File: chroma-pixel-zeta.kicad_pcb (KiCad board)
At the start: 4 copper layers, 138 x 93.2 mm, 151 parts, among them J1 Micro_SD_Card_Det_Hirose_DM3AT, J10 Conn_01x24_MountingPin, J11 AudioJack3, J12 USB_A, J14 LCD_TP_I2C, J15 LCD_SPI, J2 TFT_LCD, J4 USB-C, J5 I2C-STEMMA-QT, J6 BAT, J7 swd, J8 SPKR, J9 UART, SW1 SW_Push, SW2 SW_Push, SW3 SW_Push, SW4 SW_Push, U1 MT25Q, U10 PCM5102A, U11 TLV75733PDBV, U2 STM32H743IITx, U4 MT25Q, U5 TPS61169, U6 MAX98357AETE_, U7 CAT24C128, U8 TLV75733PDBV, U9 MT48LC16M16A2P, Y1 25MHz, Y2 32.768KHz

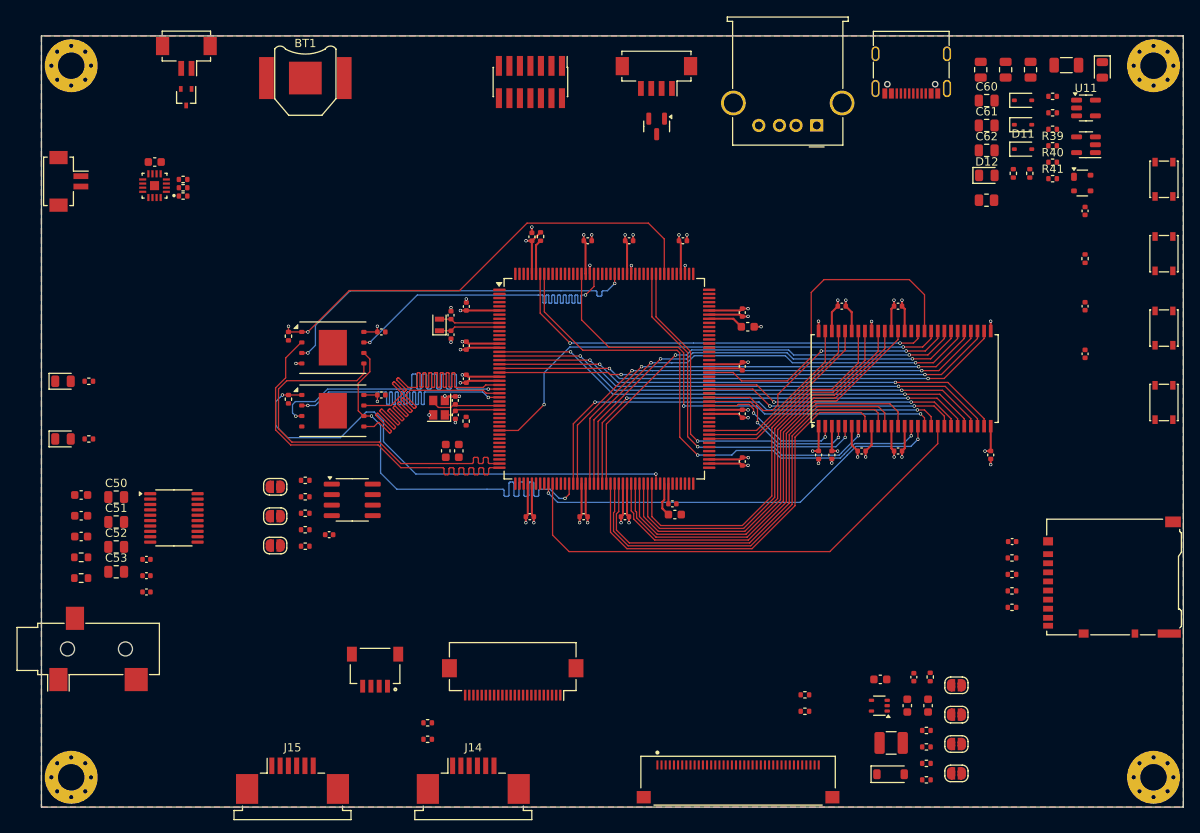
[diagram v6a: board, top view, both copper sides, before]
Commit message: finished layout backlight driver
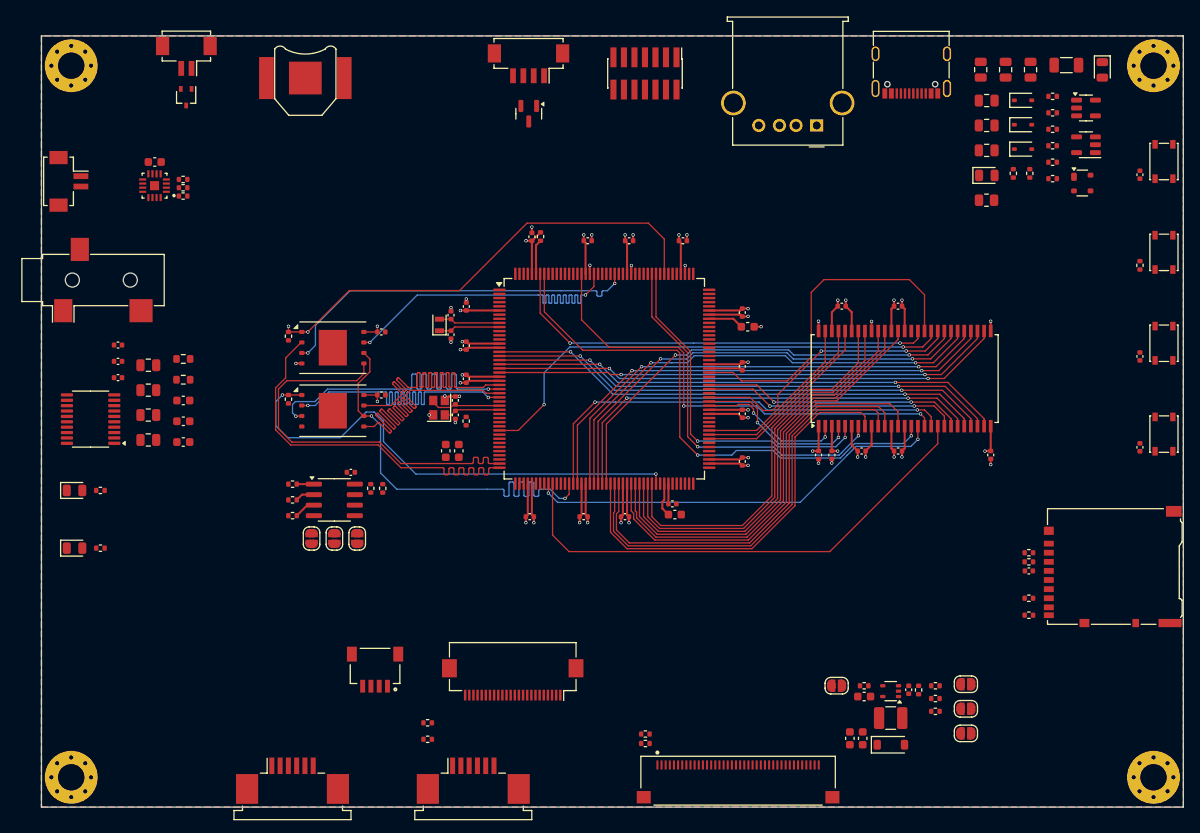
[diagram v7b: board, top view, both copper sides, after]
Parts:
- moved J11 44.6 mm to (84.8, 71.8)
- moved C59 30.0 mm to (87.9, 79.7), turned to 180 degrees
- moved R38 29.2 mm to (95.7, 81.4), turned to 180 degrees
- moved C57 26.1 mm to (87.9, 81.7), turned to 180 degrees
- moved C53 25.3 mm to (91.5, 82.1), turned to 180 degrees
- moved R37 24.8 mm to (95.7, 83.9), turned to 180 degrees
- moved C55 22.2 mm to (87.9, 83.6), turned to 180 degrees
- moved C58 20.6 mm to (95.7, 86.4), turned to 180 degrees
- moved R35 19.9 mm to (151.6, 126.7)
- moved R36 19.7 mm to (151.6, 127.8)
- moved C52 19.3 mm to (91.5, 85.1), turned to 180 degrees
- moved C56 16.8 mm to (95.7, 88.9), turned to 180 degrees
- moved U10 15.6 mm to (84.5, 88.6), turned to 180 degrees
- moved D9 15.5 mm to (137.5, 51.7)
- moved J9 15.5 mm to (137.5, 45.7)
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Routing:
- net Net-(JP7-A): track 0.00 -> 2.59 mm
- net Net-(JP6-A): track 0.00 -> 2.33 mm
- net Net-(JP5-A): track 0.00 -> 2.06 mm

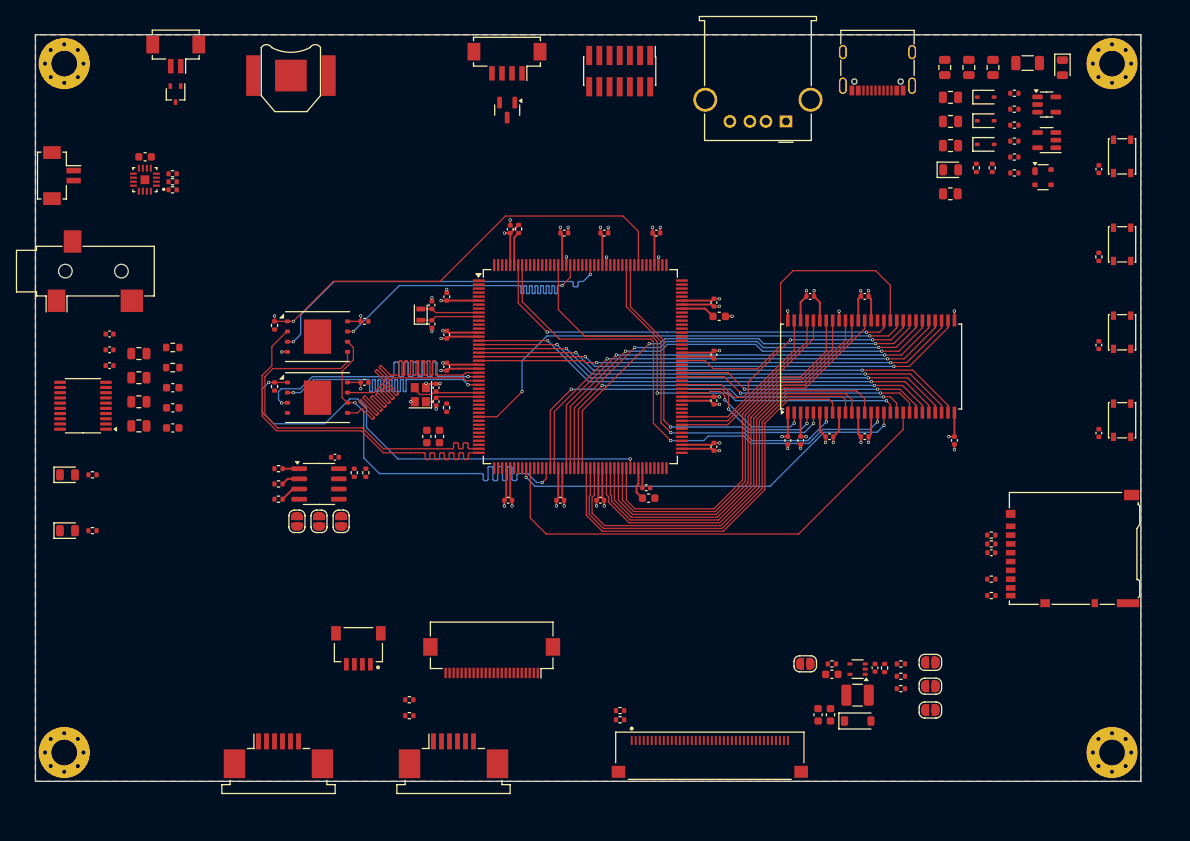
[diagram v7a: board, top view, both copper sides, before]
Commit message: Changes: USB C to midmount, CR1220 socket, flip MCU to shorten the LCD traces
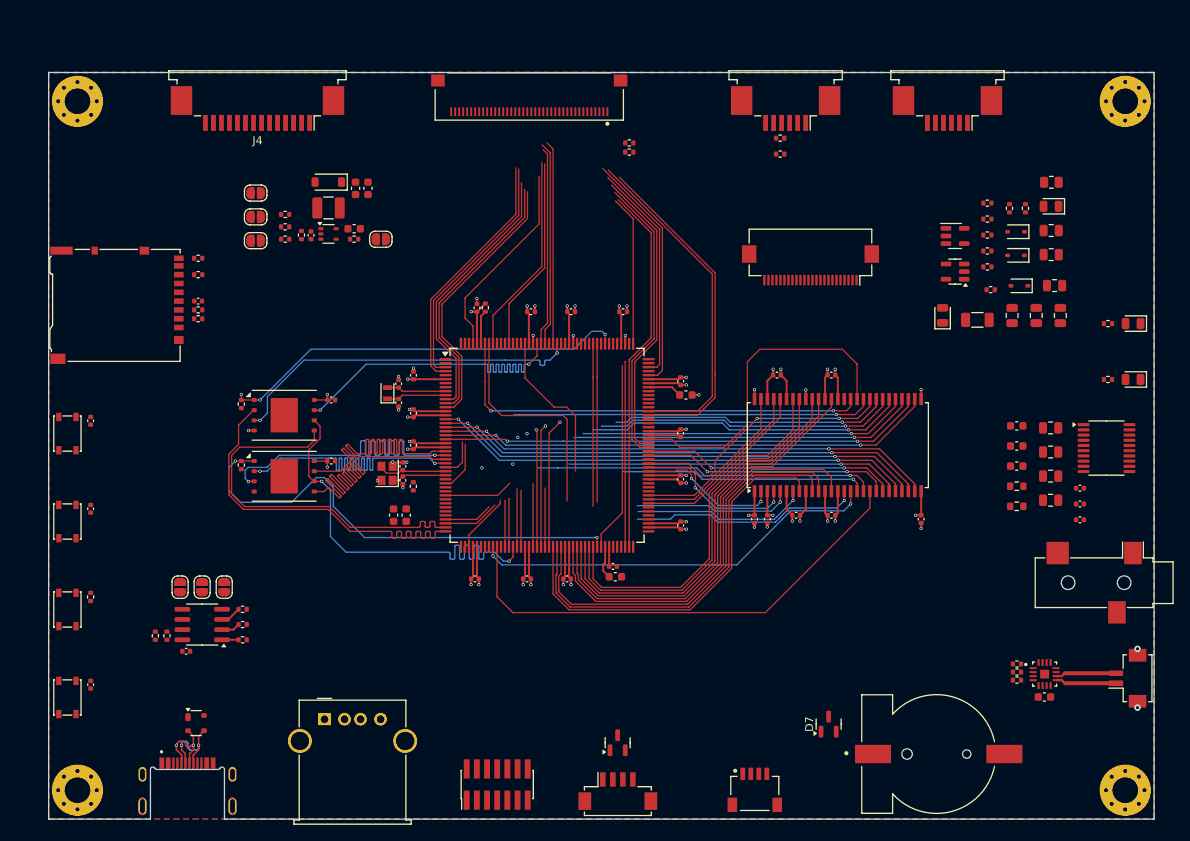
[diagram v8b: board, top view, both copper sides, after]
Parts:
- removed BT1: Battery_Cell, Battery:BatteryHolder_Keystone_2998_1x6.8mm
- removed J6: BAT, Connector_Hirose:Hirose_DF13C_CL535-0402-2-51_1x02-1MP_P1.25mm_Vertical
- added BT2: S8411-45R, CR1220-Batt-conn-S8411-45R:CR1220-Batt-conn-S8411-45R, F.Cu at (191.1, 132.1)
- added J3: 2169900003, USB_C_Mid_mount_MOLEX_2169900003:USB_C_Mid_mount_MOLEX_2169900003, F.Cu at (97.6, 138.6)
- D7: footprint Package_TO_SOT_SMD:SOT-323_SC-70 -> Package_TO_SOT_SMD:SOT-23
- J4: value USB-C -> SPI_LCD; footprint Connector_USB:USB_C_Receptacle_G-Switch_GT-USB-7010ASV -> Connector_FFC-FPC:TE_1-84953-4_1x14-1MP_P1.0mm_Horizontal
- moved H1 160.5 mm to (214.6, 136.6), turned to 0 degrees
- moved H4 157.8 mm to (83.8, 136.6), turned to -90 degrees
- moved H2 155.4 mm to (214.6, 50.6), turned to 0 degrees
- moved H3 152.6 mm to (83.8, 50.6), turned to 180 degrees
- moved SW1 148.0 mm to (82.6, 125.1), turned to -90 degrees
- moved J8 147.1 mm to (214.9, 122.7), turned to 90 degrees
- moved C24 141.4 mm to (85.5, 123.5), turned to -90 degrees
- moved SW2 139.3 mm to (82.6, 114.1), turned to -90 degrees
- moved D6 135.5 mm to (215.6, 78.4), turned to 180 degrees
- moved SW3 133.8 mm to (82.6, 103.1), turned to -90 degrees
- moved D5 133.6 mm to (215.6, 85.4), turned to 180 degrees
- moved J11 133.0 mm to (212.0, 110.7), turned to -90 degrees
- moved R18 132.8 mm to (85.5, 112.5), turned to -90 degrees
- moved SW4 131.7 mm to (82.6, 92.1), turned to -90 degrees
- moved C23 131.0 mm to (204.6, 125.0), turned to 180 degrees
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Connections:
- J14 pad 1: unconnected-(J14-Pin_1-Pad1) -> GND
- J14 pad 2: unconnected-(J14-Pin_2-Pad2) -> /LCD/LCD_TP_INT
- J14 pad 3: unconnected-(J14-Pin_3-Pad3) -> /LCD/LCD_TP_RST
- J14 pad 4: unconnected-(J14-Pin_4-Pad4) -> +3V3
- J14 pad 5: unconnected-(J14-Pin_5-Pad5) -> /LCD/LCD_TP_SCL
- J14 pad 6: unconnected-(J14-Pin_6-Pad6) -> /LCD/LCD_TP_SDA
- J14 pad MP: unconnected-(J14-MountPin-PadMP) -> GND
- J2 pad 13: /LCD/LCD_B7 -> /LCD/LTDC_B7
- J2 pad 14: /LCD/LCD_B6 -> /LCD/LTDC_B6
- J2 pad 15: /LCD/LCD_B5 -> /LCD/LTDC_B5
- J2 pad 16: /LCD/LCD_B4 -> /LCD/LTDC_B4
- J2 pad 17: /LCD/LCD_B3 -> /LCD/LTDC_B3
- J2 pad 18: /LCD/LCD_B2 -> /LCD/LTDC_B2
- J2 pad 19: /LCD/LCD_B1 -> /LCD/LTDC_B1
- J2 pad 20: /LCD/LCD_B0 -> /LCD/LTDC_B0
- J2 pad 21: /LCD/LCD_G7 -> /LCD/LTDC_G7
- J2 pad 22: /LCD/LCD_G6 -> /LCD/LTDC_G6
- J2 pad 23: /LCD/LCD_G5 -> /LCD/LTDC_G5
- J2 pad 24: /LCD/LCD_G4 -> /LCD/LTDC_G4
- J2 pad 25: /LCD/LCD_G3 -> /LCD/LTDC_G3
- J2 pad 26: /LCD/LCD_G2 -> /LCD/LTDC_G2
- J2 pad 27: /LCD/LCD_G1 -> /LCD/LTDC_G1
- J2 pad 28: /LCD/LCD_G0 -> /LCD/LTDC_G0
- J2 pad 29: /LCD/LCD_R7 -> /LCD/LTDC_R7
- J2 pad 30: /LCD/LCD_R6 -> /LCD/LTDC_R6
- J2 pad 31: /LCD/LCD_R5 -> /LCD/LTDC_R5
- J2 pad 32: /LCD/LCD_R4 -> /LCD/LTDC_R4
- J2 pad 33: /LCD/LCD_R3 -> /LCD/LTDC_R3
- J2 pad 34: /LCD/LCD_R2 -> /LCD/LTDC_R2
- J2 pad 35: /LCD/LCD_R1 -> /LCD/LTDC_R1
- J2 pad 36: /LCD/LCD_R0 -> /LCD/LTDC_R0
- R11 pad 1: GND -> Net-(J3-CC2)
- R11 pad 2: Net-(J4-CC1) -> GND
- R12 pad 2: Net-(J4-CC2) -> Net-(J3-CC1)
- R33 pad 2: /LCD/LCD_TP_SCL -> /LCD/LCD_TP_SDA
- R34 pad 2: /LCD/LCD_TP_SDA -> /LCD/LCD_TP_SCL
- U2 pad 100: unconnected-(U2-PD12-Pad100) -> /AUDIO/DIN
- U2 pad 11: unconnected-(U2-PI9-Pad11) -> /LCD/LTDC_VSYNC
- U2 pad 110: unconnected-(U2-PG6-Pad110) -> /LCD/LTDC_R7
- U2 pad 111: unconnected-(U2-PG7-Pad111) -> /LCD/LTDC_CLK
- U2 pad 118: unconnected-(U2-PC9-Pad118) -> /LCD/LTDC_G3
- U2 pad 119: unconnected-(U2-PA8-Pad119) -> /LCD/LTDC_B3
- U2 pad 12: unconnected-(U2-PI10-Pad12) -> /LCD/LTDC_HSYNC
- U2 pad 122: unconnected-(U2-PA11-Pad122) -> /USB/USB_D-
- U2 pad 123: unconnected-(U2-PA12-Pad123) -> /USB/USB_D+
- U2 pad 128: unconnected-(U2-PH13-Pad128) -> /LCD/LTDC_G2
- U2 pad 13: unconnected-(U2-PI11-Pad13) -> /LCD/LTDC_G6
- U2 pad 130: unconnected-(U2-PH15-Pad130) -> /LCD/LTDC_G4
- U2 pad 133: unconnected-(U2-PI2-Pad133) -> /LCD/LTDC_G7
- U2 pad 138: unconnected-(U2-PA15-Pad138) -> /AUDIO/LRCK
- U2 pad 139: unconnected-(U2-PC10-Pad139) -> /AUDIO/BCK
- U2 pad 151: unconnected-(U2-PD7-Pad151) -> /AUDIO/I2S_SDO
- U2 pad 153: unconnected-(U2-PG10-Pad153) -> /LCD/LTDC_B2
- U2 pad 154: unconnected-(U2-PG11-Pad154) -> /MEMORY SD CARD/SD_DAT2
- U2 pad 155: unconnected-(U2-PG12-Pad155) -> /LCD/LTDC_B1
- U2 pad 156: unconnected-(U2-PG13-Pad156) -> /LCD/LTDC_R0
- U2 pad 162: unconnected-(U2-PB4-Pad162) -> /MEMORY SD CARD/SD_DAT3
- U2 pad 164: unconnected-(U2-PB6-Pad164) -> /LCD/LTDC_B6
- U2 pad 168: unconnected-(U2-PB9-Pad168) -> /LCD/LTDC_B7
- U2 pad 173: unconnected-(U2-PI4-Pad173) -> /LCD/LTDC_B4
- U2 pad 28: unconnected-(U2-PF10-Pad28) -> /LCD/LTDC_DE
- U2 pad 3: unconnected-(U2-PE4-Pad3) -> /LCD/LTDC_B0
- U2 pad 32: unconnected-(U2-PC0-Pad32) -> /LCD/LTDC_R5
- U2 pad 33: unconnected-(U2-PC1-Pad33) -> /MEMORY SD CARD/SD_CLK
- U2 pad 4: unconnected-(U2-PE5-Pad4) -> /LCD/LTDC_G0
- U2 pad 40: unconnected-(U2-PA0-Pad40) -> /MEMORY SD CARD/SD_CMD
- U2 pad 41: unconnected-(U2-PA1-Pad41) -> /LCD/LTDC_R2
- U2 pad 42: unconnected-(U2-PA2-Pad42) -> /LCD/LTDC_R1
- U2 pad 47: unconnected-(U2-PA3-Pad47) -> /LCD/LTDC_B5
- U2 pad 50: unconnected-(U2-PA4-Pad50) -> /AUDIO/I2S_WS
- U2 pad 51: unconnected-(U2-PA5-Pad51) -> /AUDIO/I2S_CK
- U2 pad 56: unconnected-(U2-PB0-Pad56) -> /LCD/LTDC_G1
- U2 pad 57: unconnected-(U2-PB1-Pad57) -> /LCD/LTDC_R6
- U2 pad 80: unconnected-(U2-PB11-Pad80) -> /LCD/LTDC_G5
- U2 pad 86: unconnected-(U2-PH9-Pad86) -> /LCD/LTDC_R3
- U2 pad 87: unconnected-(U2-PH10-Pad87) -> /LCD/LTDC_R4
- U2 pad 94: unconnected-(U2-PB14-Pad94) -> /MEMORY SD CARD/SD_DAT0
- U2 pad 95: unconnected-(U2-PB15-Pad95) -> /MEMORY SD CARD/SD_DAT1
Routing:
- net /LCD/LTDC_R4: track 0.00 -> 46.2 mm
- net /LCD/LTDC_B3: track 0.00 -> 42.4 mm
- net /LCD/LTDC_G3: track 0.00 -> 41.7 mm
- net /LCD/LTDC_CLK: track 0.00 -> 37.1 mm
- net /LCD/LTDC_R7: track 0.00 -> 36.4 mm
- net /LCD/LTDC_G6: track 0.00 -> 33.8 mm
- net /LCD/LTDC_VSYNC: track 0.00 -> 33.6 mm
- net /LCD/LTDC_HSYNC: track 0.00 -> 33.4 mm
- net /LCD/LTDC_G0: track 0.00 -> 31.3 mm
- net /LCD/LTDC_B0: track 0.00 -> 30.5 mm
- net /LCD/LTDC_G2: track 0.00 -> 30.2 mm
- net /LCD/LTDC_G4: track 0.00 -> 27.5 mm
- net /LCD/LTDC_B1: track 0.00 -> 25.5 mm
- net /LCD/LTDC_B2: track 0.00 -> 25.4 mm
- net /LCD/LTDC_B7: track 0.00 -> 25.1 mm
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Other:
- outline, holes or cut-outs redrawn
